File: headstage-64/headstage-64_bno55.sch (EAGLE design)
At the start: 201 parts, among them J8 DF40C-70DP-0.4V(51), J9 PINHD-1X5_HALF_CONNETOR, U1 ADA4062-4ACPZ-R7, U10 DS90UB913A_WQFN, U11 TS4231, U12 TS4231, U13 TLV70733, U14 10M08DC, U15 TLV70733, U16 LT3463, U17 TLV70725, U18 TPS62621, U19 ASCO-50.000MHZ-EK-T3, U2 AD5681RBCPZ-1RL7, U20 TLV70712, U21 BNO055, U3 CAT4016_QFN, U4 TPL0501_UQFN, U5 DG509B, U6 TS4231, U8 RHD2064_BGA, U9 TS4231, Y2 ECS-.327-12.5-1210-TR

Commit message: WIP routing for BNO055 variant - Removed a few decoupling caps to amke space - Signals still not routed, and a bunch of cleanup needed
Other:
- moved on the sheet: C4, C76
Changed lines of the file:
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@@
 <attribute name="PARTNO" x="568.96" y="154.94" size="1.27" layer="96" rot="R90" display="off"/>
 </instance>
-<instance part="C4" gate="C" x="662.94" y="685.8">
-<attribute name="PARTNO" x="662.94" y="685.8" size="1.27" layer="96" display="off"/>
+<instance part="C4" gate="C" x="701.04" y="739.14">
+<attribute name="PARTNO" x="701.04" y="739.14" size="1.27" layer="96" display="off"/>
 </instance>
 <instance part="C6" gate="C" x="756.92" y="668.02" rot="R90">
@@
 <instance part="U1" gate="C" x="469.9" y="673.1"/>
 <instance part="U1" gate="B" x="469.9" y="637.54" rot="MR180"/>
-<instance part="C76" gate="C" x="223.52" y="398.78" rot="MR0"/>
+<instance part="C76" gate="C" x="241.3" y="330.2" rot="MR0"/>
 <instance part="C77" gate="C" x="213.36" y="398.78" rot="MR0">
 <attribute name="PARTNO" x="213.36" y="398.78" size="1.27" layer="96" rot="MR0" display="off"/>
@@
 <wire x1="662.94" y1="678.18" x2="645.16" y2="678.18" width="0.1524" layer="91"/>
 <wire x1="645.16" y1="678.18" x2="645.16" y2="660.4" width="0.1524" layer="91"/>
-<wire x1="662.94" y1="678.18" x2="662.94" y2="680.72" width="0.1524" layer="91"/>
+<wire x1="662.94" y1="678.18" x2="701.04" y2="734.06" width="0.1524" layer="91"/>
 <junction x="662.94" y="678.18"/>
 <pinref part="SUPPLY21" gate="PE" pin="GND"/>
@@
 <segment>
 <pinref part="C76" gate="C" pin="2"/>
-<wire x1="223.52" y1="393.7" x2="223.52" y2="391.16" width="0.1524" layer="91"/>
+<wire x1="241.3" y1="325.12" x2="223.52" y2="391.16" width="0.1524" layer="91"/>
 <pinref part="C77" gate="C" pin="2"/>
 <wire x1="213.36" y1="355.6" x2="213.36" y2="365.76" width="0.1524" layer="91"/>
@@
 <segment>
 <pinref part="C76" gate="C" pin="1"/>
-<wire x1="223.52" y1="401.32" x2="223.52" y2="408.94" width="0.1524" layer="91"/>
+<wire x1="241.3" y1="332.74" x2="223.52" y2="408.94" width="0.1524" layer="91"/>
 <wire x1="264.16" y1="408.94" x2="228.6" y2="408.94" width="0.1524" layer="91"/>
 <pinref part="C77" gate="C" pin="1"/>
@@
 <wire x1="662.94" y1="690.88" x2="645.16" y2="690.88" width="0.1524" layer="91"/>
 <wire x1="645.16" y1="690.88" x2="645.16" y2="693.42" width="0.1524" layer="91"/>
-<wire x1="662.94" y1="688.34" x2="662.94" y2="690.88" width="0.1524" layer="91"/>
+<wire x1="701.04" y1="741.68" x2="662.94" y2="690.88" width="0.1524" layer="91"/>
 <junction x="662.94" y="690.88"/>
 <pinref part="C4" gate="C" pin="1"/>

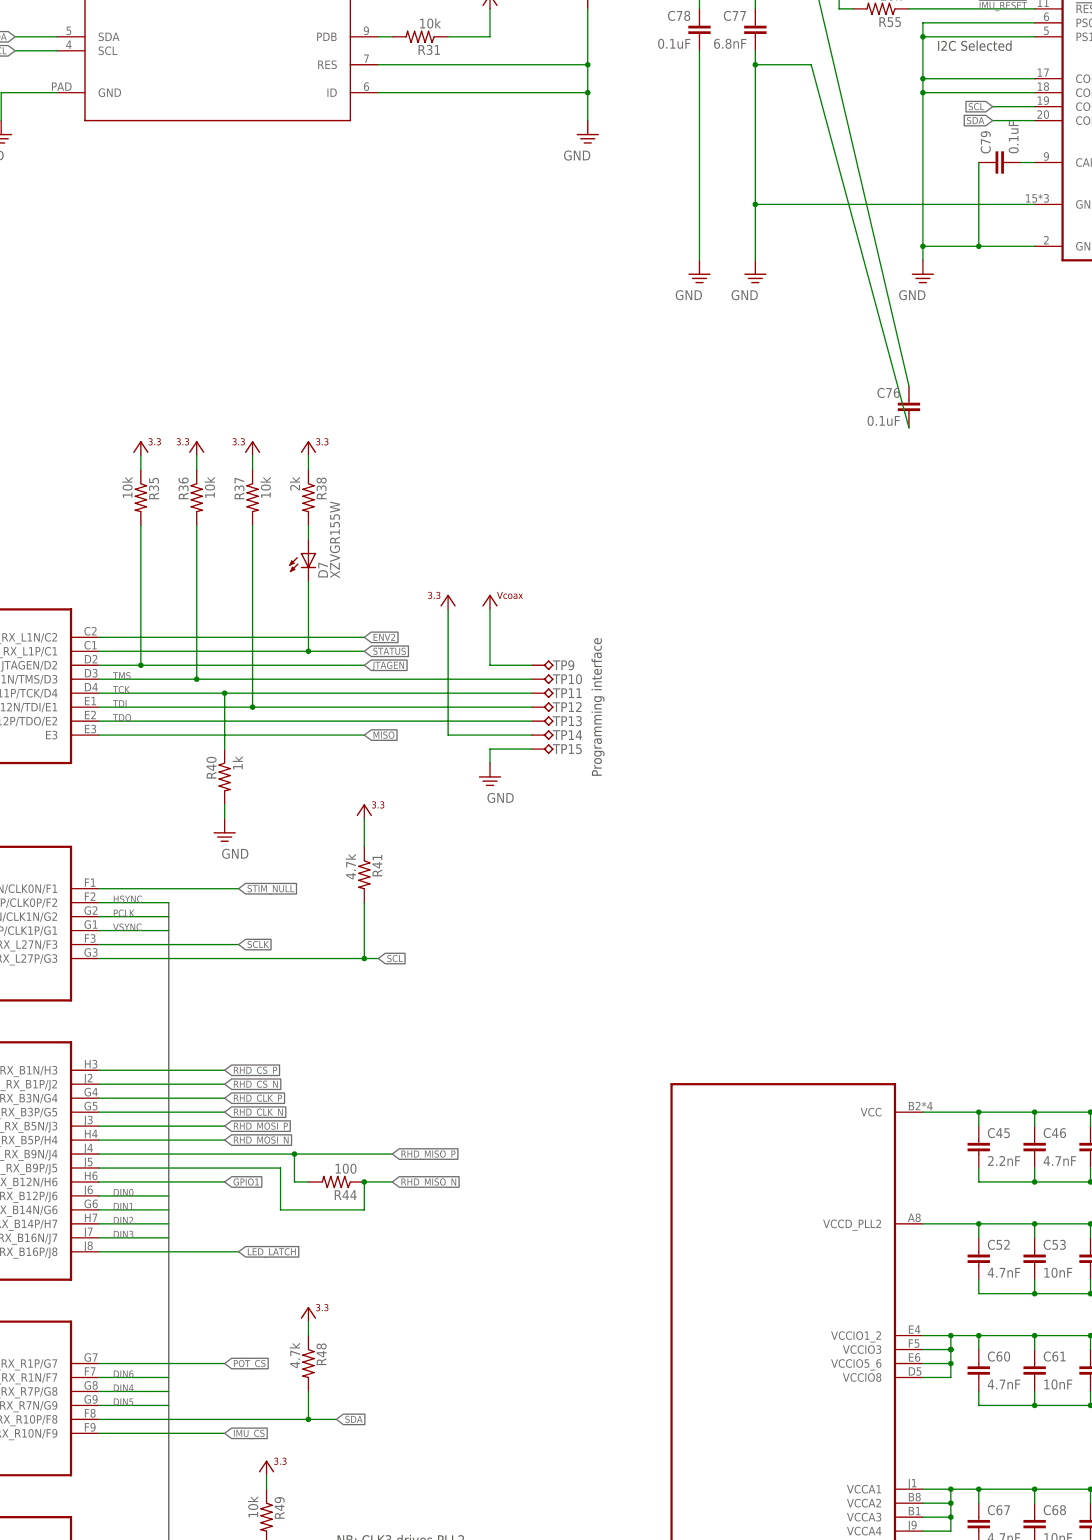
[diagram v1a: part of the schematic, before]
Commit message: Cleaned up layout for BNO55 variant - Needs a proper DRM etc
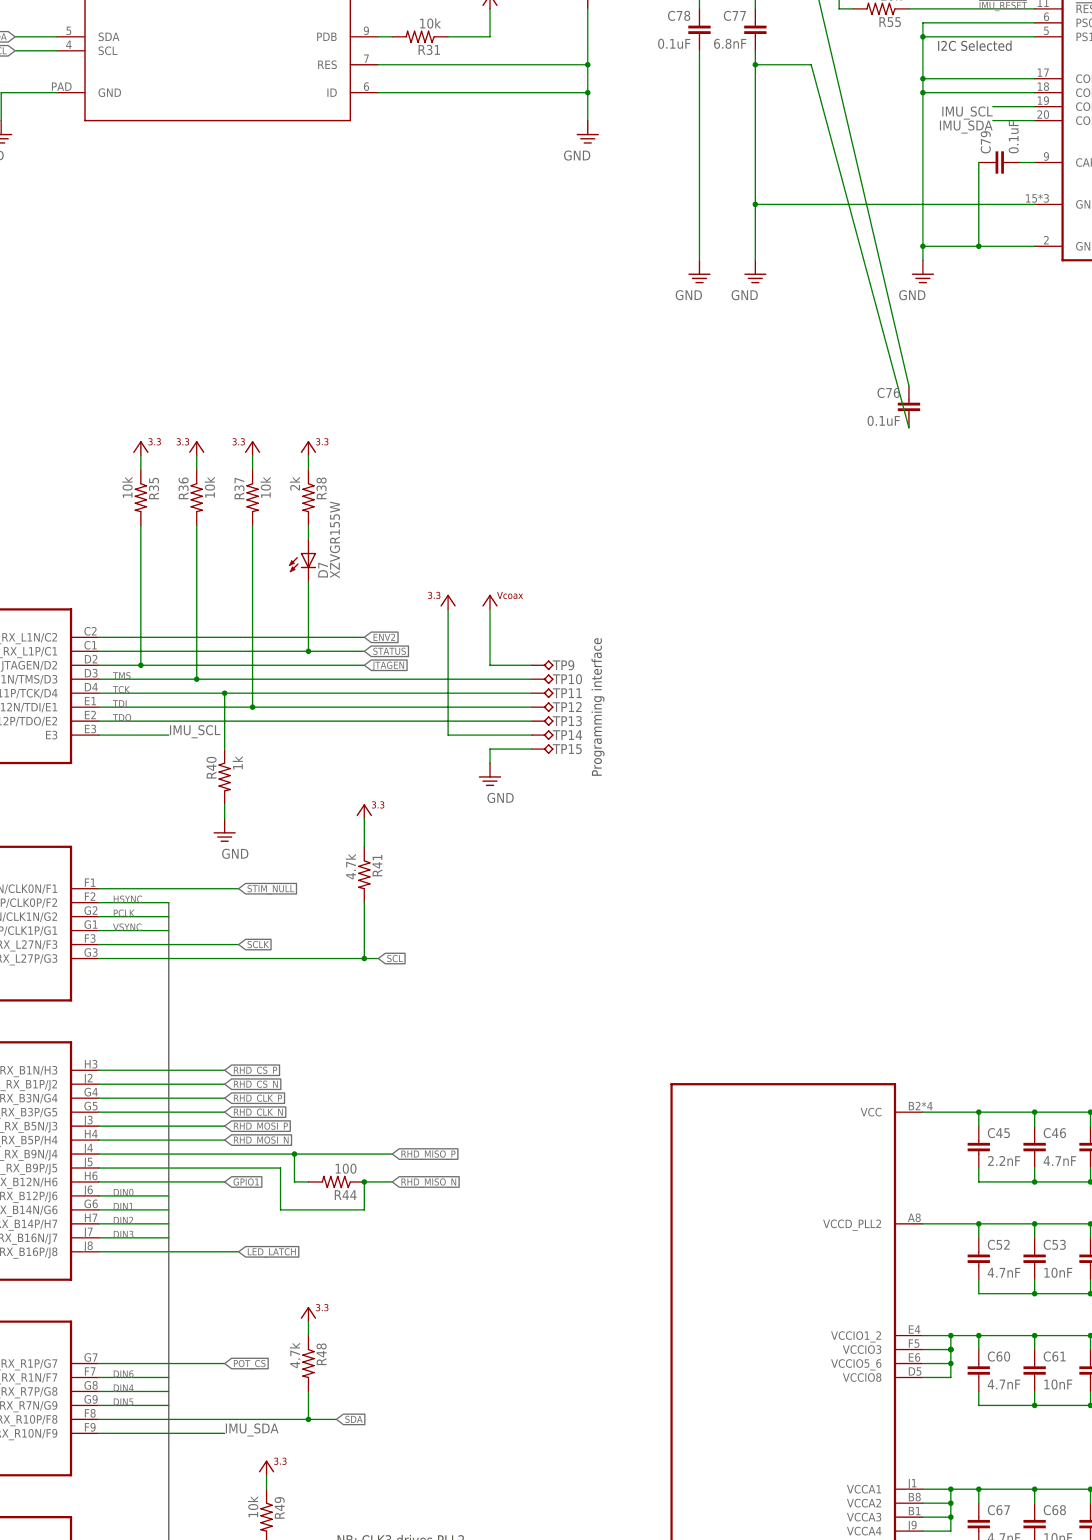
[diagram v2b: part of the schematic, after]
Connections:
- removed net IMU_CS: U14G$4.DIFFIO_RX_R10N/F9
- removed net MISO: U14G$1.E3
- new net IMU_SCL: U14G$1.E3, U21.COM1/SCL/RX
- new net IMU_SDA: U14G$4.DIFFIO_RX_R10N/F9, U21.COM0/SDA/TX
- net SCL: no longer U21.COM1/SCL/RX
- net SDA: no longer U21.COM0/SDA/TX
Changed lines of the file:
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@@
 <?xml version="1.0" encoding="utf-8"?>
 <!DOCTYPE eagle SYSTEM "eagle.dtd">
-<eagle version="9.0.1">
+<eagle version="8.4.0">
 <drawing>
 <settings>
@@
 <junction x="142.24" y="228.6"/>
 </segment>
-<segment>
-<pinref part="U21" gate="G$1" pin="COM1/SCL/RX"/>
-<wire x1="264.16" y1="383.54" x2="256.54" y2="383.54" width="0.1524" layer="91"/>
-<label x="256.54" y="383.54" size="1.27" layer="95" rot="R180" xref="yes"/>
-</segment>
 </net>
 <net name="SDA" class="0">
@@
 <junction x="132.08" y="144.78"/>
 </segment>
-<segment>
-<pinref part="U21" gate="G$1" pin="COM0/SDA/TX"/>
-<wire x1="264.16" y1="381" x2="256.54" y2="381" width="0.1524" layer="91"/>
-<label x="256.54" y="381" size="1.27" layer="95" rot="R180" xref="yes"/>
-</segment>
 </net>
 <net name="N$34" class="0">
@@
 </segment>
 </net>
-<net name="IMU_CS" class="0">
-<segment>
-<label x="116.84" y="142.24" size="1.27" layer="95" xref="yes"/>
-<wire x1="116.84" y1="142.24" x2="93.98" y2="142.24" width="0.1524" layer="91"/>
-<pinref part="U14" gate="G$4" pin="DIFFIO_RX_R10N/F9"/>
-</segment>
-</net>
 <net name="LED_LATCH" class="0">
 <segment>
@@
 </segment>
 </net>
-<net name="MISO" class="0">
-<segment>
-<pinref part="U14" gate="G$1" pin="E3"/>
-<wire x1="93.98" y1="269.24" x2="142.24" y2="269.24" width="0.1524" layer="91"/>
-<label x="142.24" y="269.24" size="1.27" layer="95" xref="yes"/>
-</segment>
-</net>
 <net name="N$53" class="0">
 <segment>
@@
 </segment>
 </net>
+<net name="IMU_SCL" class="0">
+<segment>
+<pinref part="U21" gate="G$1" pin="COM1/SCL/RX"/>
+<wire x1="264.16" y1="383.54" x2="256.54" y2="383.54" width="0.1524" layer="91"/>
+<label x="256.54" y="383.54" size="1.778" layer="95" rot="R180"/>
+</segment>
+<segment>
+<pinref part="U14" gate="G$1" pin="E3"/>
+<wire x1="93.98" y1="269.24" x2="106.68" y2="269.24" width="0.1524" layer="91"/>
+<label x="106.68" y="269.24" size="1.778" layer="95"/>
+</segment>
+</net>
+<net name="IMU_SDA" class="0">
+<segment>
+<pinref part="U21" gate="G$1" pin="COM0/SDA/TX"/>
+<wire x1="264.16" y1="381" x2="256.54" y2="381" width="0.1524" layer="91"/>
+<label x="256.54" y="381" size="1.778" layer="95" rot="R180"/>
+</segment>
+<segment>
+<pinref part="U14" gate="G$4" pin="DIFFIO_RX_R10N/F9"/>
+<wire x1="93.98" y1="142.24" x2="116.84" y2="142.24" width="0.1524" layer="91"/>
+<label x="116.84" y="142.24" size="1.778" layer="95"/>
+</segment>
+</net>

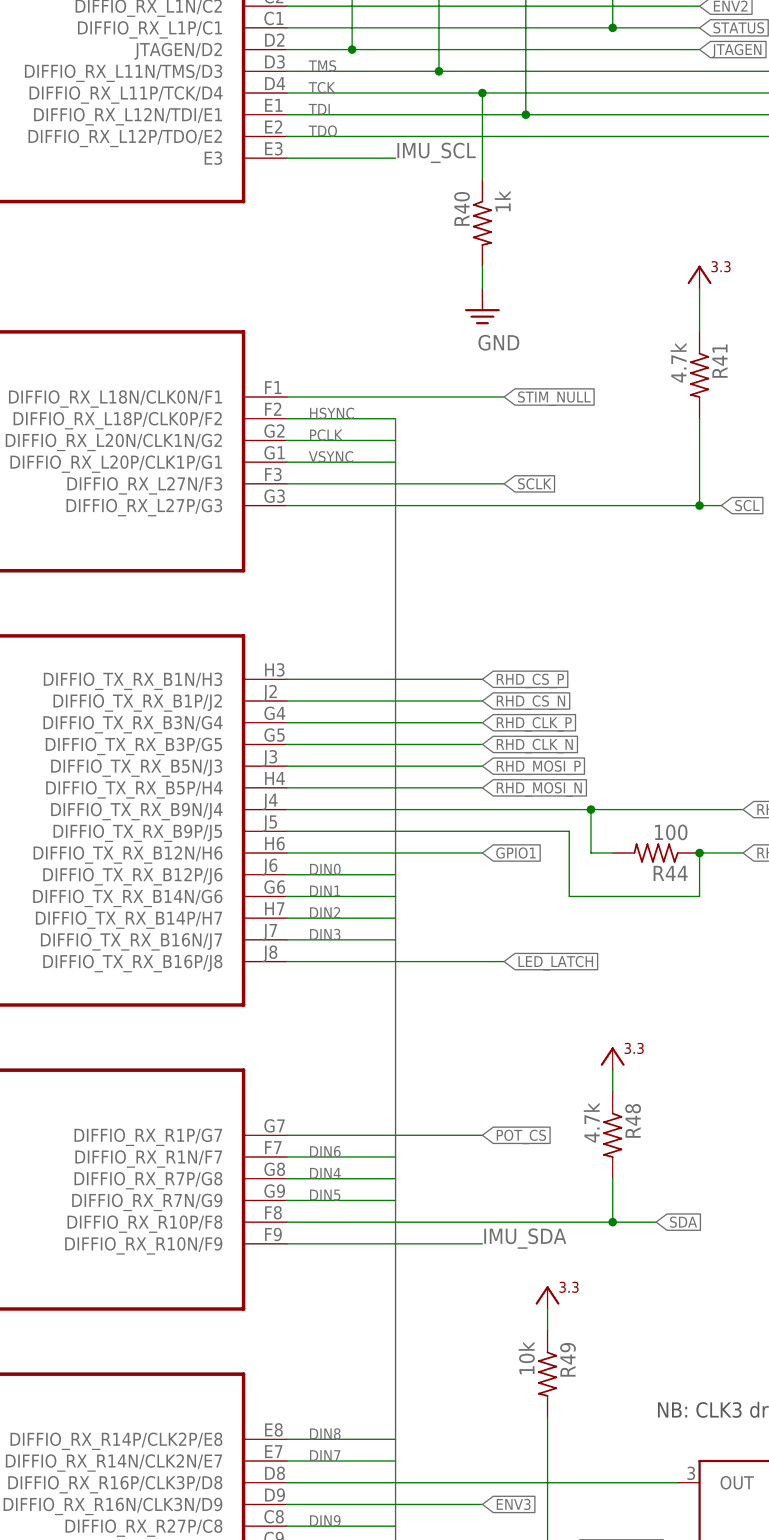
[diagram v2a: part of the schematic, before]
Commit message: Added pullups to secondary i2c bus for IMU (WIP)
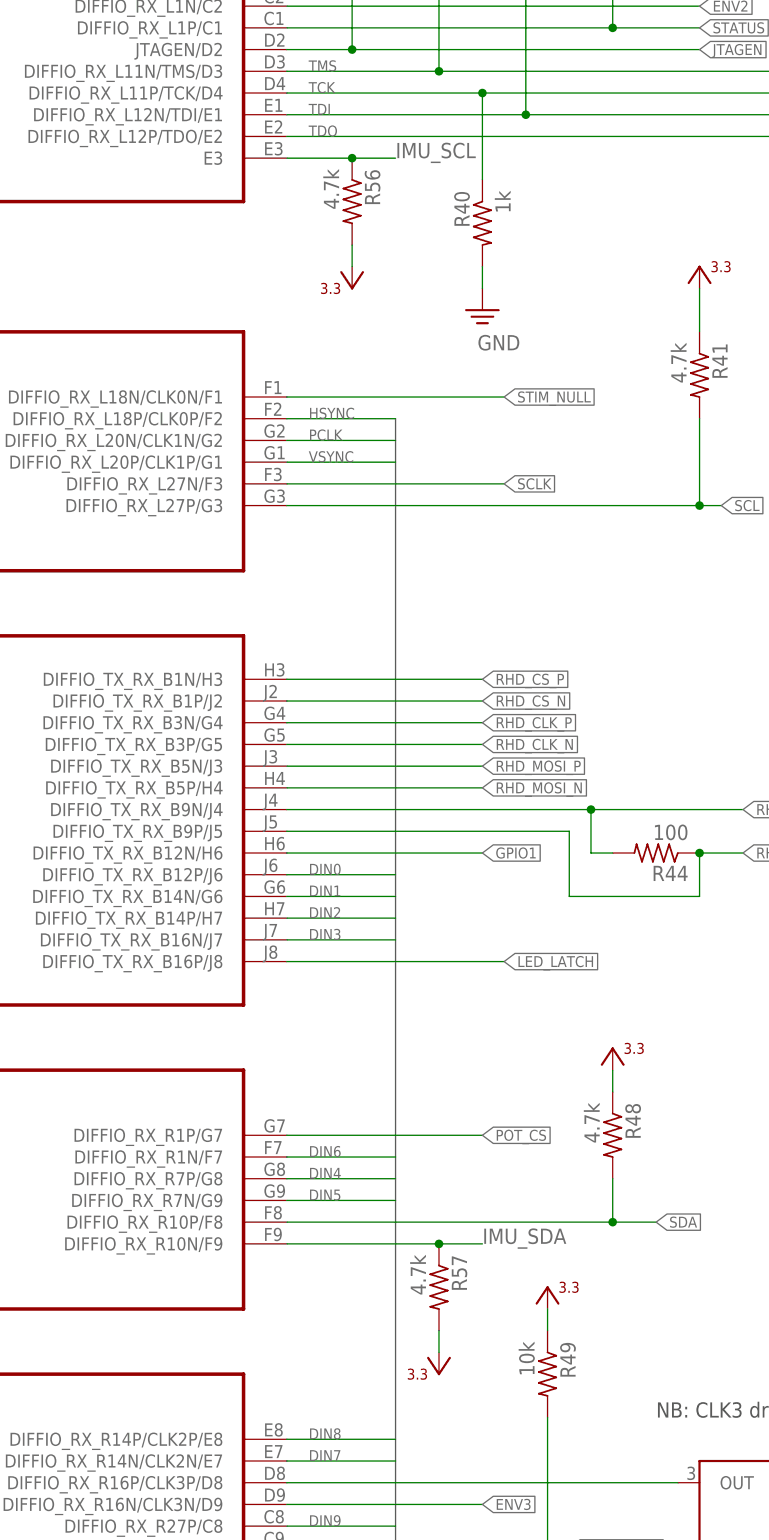
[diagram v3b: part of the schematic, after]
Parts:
- added R56, R57: 4.7k, jonnew:R_0201T
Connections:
- net +3V3: now also R56.2, R57.2
- net IMU_SCL: now also R56.1
- net IMU_SDA: now also R57.1
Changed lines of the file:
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@@
 <part name="C81" library="jonnew" deviceset="C" device="_0402T" value="22pF, NP0 2%"/>
 <part name="GND37" library="jonnew" deviceset="GND" device=""/>
+<part name="R56" library="jonnew" deviceset="R" device="_0201T" value="4.7k"/>
+<part name="U$19" library="jonnew" deviceset="+3V3" device=""/>
+<part name="R57" library="jonnew" deviceset="R" device="_0201T" value="4.7k"/>
+<part name="U$40" library="jonnew" deviceset="+3V3" device=""/>
 </parts>
 <sheets>
@@
 <instance part="C81" gate="C" x="347.98" y="370.84"/>
 <instance part="GND37" gate="PE" x="337.82" y="353.06"/>
+<instance part="R56" gate="R" x="101.6" y="264.16" rot="R270"/>
+<instance part="U$19" gate="PWR1" x="101.6" y="256.54" rot="R180"/>
+<instance part="R57" gate="R" x="111.76" y="137.16" rot="R270"/>
+<instance part="U$40" gate="PWR1" x="111.76" y="129.54" rot="R180"/>
 </instances>
 <busses>
@@
 <wire x1="325.12" y1="424.18" x2="325.12" y2="426.72" width="0.1524" layer="91"/>
 </segment>
+<segment>
+<pinref part="R56" gate="R" pin="2"/>
+<pinref part="U$19" gate="PWR1" pin="+3V3"/>
+<wire x1="101.6" y1="256.54" x2="101.6" y2="259.08" width="0.1524" layer="91"/>
+</segment>
+<segment>
+<pinref part="R57" gate="R" pin="2"/>
+<pinref part="U$40" gate="PWR1" pin="+3V3"/>
+<wire x1="111.76" y1="129.54" x2="111.76" y2="132.08" width="0.1524" layer="91"/>
+</segment>
 </net>
 <net name="LED-2" class="0">
@@
 <segment>
 <pinref part="U14" gate="G$1" pin="E3"/>
-<wire x1="93.98" y1="269.24" x2="106.68" y2="269.24" width="0.1524" layer="91"/>
+<wire x1="93.98" y1="269.24" x2="101.6" y2="269.24" width="0.1524" layer="91"/>
 <label x="106.68" y="269.24" size="1.778" layer="95"/>
+<pinref part="R56" gate="R" pin="1"/>
+<wire x1="101.6" y1="269.24" x2="106.68" y2="269.24" width="0.1524" layer="91"/>
+<junction x="101.6" y="269.24"/>
 </segment>
 </net>
@@
 <segment>
 <pinref part="U14" gate="G$4" pin="DIFFIO_RX_R10N/F9"/>
-<wire x1="93.98" y1="142.24" x2="116.84" y2="142.24" width="0.1524" layer="91"/>
+<wire x1="93.98" y1="142.24" x2="111.76" y2="142.24" width="0.1524" layer="91"/>
 <label x="116.84" y="142.24" size="1.778" layer="95"/>
+<pinref part="R57" gate="R" pin="1"/>
+<wire x1="111.76" y1="142.24" x2="116.84" y2="142.24" width="0.1524" layer="91"/>
+<junction x="111.76" y="142.24"/>
 </segment>
 </net>
